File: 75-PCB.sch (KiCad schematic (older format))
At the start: 324 parts, among them J1 AVR-ISP-6, Q1 2N7002, SW1 SW_Push, U1 AT90USB1286-AU, U2 PRTR5V0U2X, Y1 16MHz

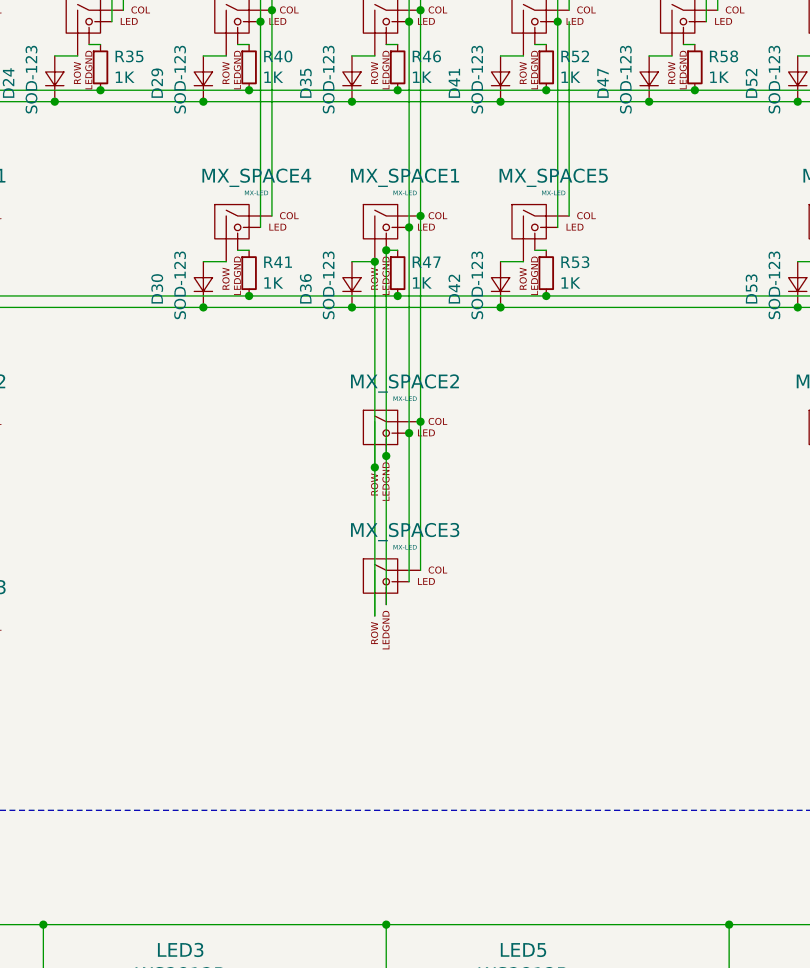
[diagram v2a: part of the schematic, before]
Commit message: Added switch for support for another bottom row layout
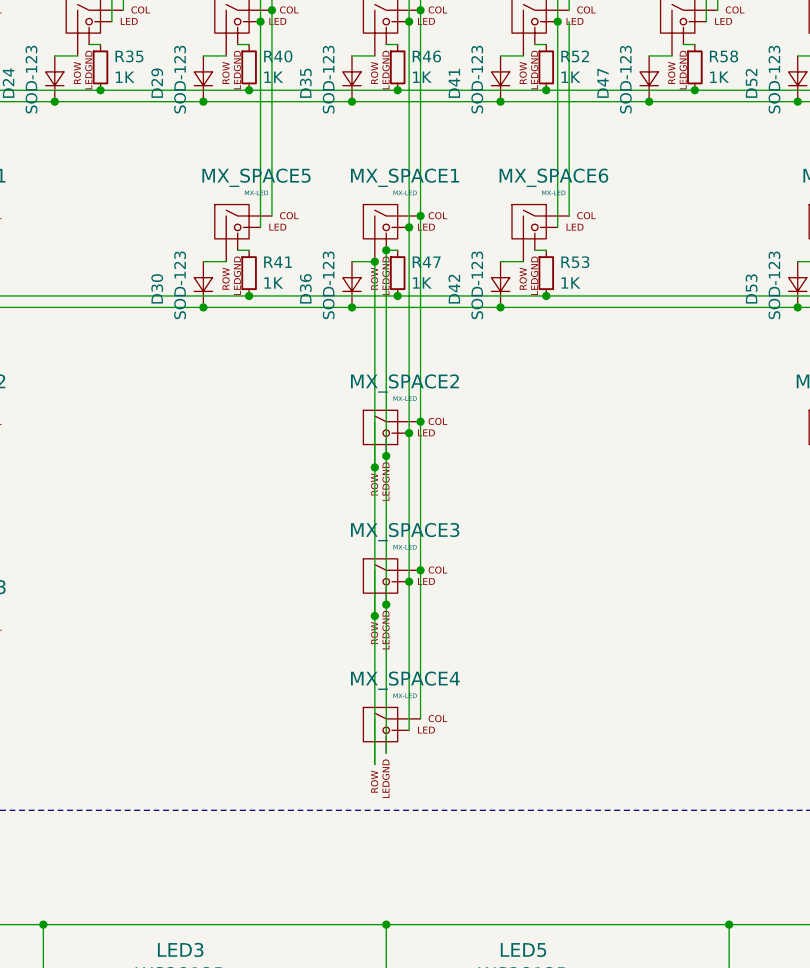
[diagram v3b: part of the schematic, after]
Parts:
- added MX_SPACE4: MX-LED, MX_Only:MXOnly-1.25U, symbol MX_Alps_Hybrid:MX-LED
- MX_SPACE3: footprint MX_Only:MXOnly-1.25U -> MX_Only:MXOnly-7U-FLIPPED-ReversedStabilizers
- renumbered MX_SPACE4 to MX_SPACE5, MX_SPACE5 to MX_SPACE6
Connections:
- net +5V: now also MX_SPACE4.3 (LED)
- net COL5: now also MX_SPACE4.1 (COL)
- net at D36.2 (A), MX_SPACE1.2 (ROW), MX_SPACE2.2 (ROW)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: now also MX_SPACE4.2 (ROW)
- net at MX_SPACE1.4 (LEDGND), MX_SPACE2.4 (LEDGND), MX_SPACE3.4 (LEDGND)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: now also MX_SPACE4.4 (LEDGND)
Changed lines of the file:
@@
 $EndComp
 $Comp
-L MX_Alps_Hybrid:MX-LED MX_SPACE4
+L MX_Alps_Hybrid:MX-LED MX_SPACE5
 U 1 1 5EA48DDC
 P 3850 5950
-F 0 "MX_SPACE4" H 3932 6174 60  0000 C CNN
+F 0 "MX_SPACE5" H 3932 6174 60  0000 C CNN
 F 1 "MX-LED" H 3932 6100 20  0000 C CNN
 F 2 "MX_Only:MXOnly-2.75U-ReversedStabilizers" H 3225 5925 60  0001 C CNN
@@
 Connection ~ 4450 6100
 $Comp
-L MX_Alps_Hybrid:MX-LED MX_SPACE5
+L MX_Alps_Hybrid:MX-LED MX_SPACE6
 U 1 1 5EE96CC6
 P 5150 5950
-F 0 "MX_SPACE5" H 5232 6174 60  0000 C CNN
+F 0 "MX_SPACE6" H 5232 6174 60  0000 C CNN
 F 1 "MX-LED" H 5232 6100 20  0000 C CNN
 F 2 "MX_Only:MXOnly-2.25U-ReversedStabilizers" H 4525 5925 60  0001 C CNN
@@
 F 0 "MX_SPACE3" H 4582 7724 60  0000 C CNN
 F 1 "MX-LED" H 4582 7650 20  0000 C CNN
-F 2 "MX_Only:MXOnly-1.25U" H 3875 7475 60  0001 C CNN
+F 2 "MX_Only:MXOnly-7U-FLIPPED-ReversedStabilizers" H 3875 7475 60  0001 C CNN
 F 3 "" H 3875 7475 60  0001 C CNN
 	1    4500 7500
@@
 	700  5200 1100 5200
 Connection ~ 1100 5200
-$Comp
-L MX_Alps_Hybrid:MX-LED MX_LCTRL3
-U 1 1 5F0D2C14
-P 1250 7750
-F 0 "MX_LCTRL3" H 1332 7974 60  0000 C CNN
-F 1 "MX-LED" H 1332 7900 20  0000 C CNN
-F 2 "MX_Only:MXOnly-1.5U" H 625 7725 60  0001 C CNN
-F 3 "" H 625 7725 60  0001 C CNN
-	1    1250 7750
-	1    0    0    -1
-$EndComp
-$Comp
-L MX_Alps_Hybrid:MX-LED MX_LALT3
-U 1 1 5F0D2C1A
-P 2550 7750
-F 0 "MX_LALT3" H 2632 7974 60  0000 C CNN
-F 1 "MX-LED" H 2632 7900 20  0000 C CNN
-F 2 "MX_Only:MXOnly-1.5U" H 1925 7725 60  0001 C CNN
-F 3 "" H 1925 7725 60  0001 C CNN
-	1    2550 7750
-	1    0    0    -1
-$EndComp
-Wire Wire Line
-	2700 7700 2700 6800
-Wire Wire Line
-	1400 7700 1400 6800
 $Comp
 L MX_Alps_Hybrid:MX-LED MX_LWIN2
@@
 	1850 6100 1850 7000
 Connection ~ 1850 6100
-Wire Wire Line
-	2500 7900 2500 7000
-Connection ~ 2500 7000
-Wire Wire Line
-	1200 7900 1200 7000
-Connection ~ 1200 7000
 $Comp
 L Device:R_Small R18
@@
 Connection ~ 1250 6050
 Wire Wire Line
-	1250 7850 1250 6950
-Connection ~ 1250 6950
-Wire Wire Line
-	2550 7850 2550 6950
-Wire Wire Line
 	2550 6950 2550 6050
-Connection ~ 2550 6950
 Connection ~ 2550 6050
 Wire Wire Line
@@
 Wire Wire Line
 	11050 6250 10400 6250
-Wire Wire Line
-	1350 7750 1350 6850
 Connection ~ 1350 1450
 Wire Wire Line
@@
 Wire Wire Line
 	1350 5950 1350 5050
-Connection ~ 1350 6850
 Wire Wire Line
 	1350 6850 1350 5950
@@
 	2000 5950 2000 6850
 Wire Wire Line
-	2650 7750 2650 6850
-Wire Wire Line
 	2650 1000 2000 1000
 Connection ~ 2650 1450
@@
 Wire Wire Line
 	2650 5950 2650 5050
-Connection ~ 2650 6850
 Wire Wire Line
 	2650 6850 2650 5950
@@
 Wire Wire Line
 	11100 5050 11100 5950
-Connection ~ 1400 6800
 Connection ~ 1750 5400
 Wire Wire Line
 	1750 5400 2400 5400
 Connection ~ 2050 5900
-Connection ~ 2700 6800
 Text GLabel 13400 4650 2    50   Input ~ 0
 RESET
@@
 	700  4300 1100 4300
 Connection ~ 1100 4300
+Connection ~ 2650 6850
+Wire Wire Line
+	2650 7750 2650 6850
+Connection ~ 1350 6850
+Wire Wire Line
+	1350 7750 1350 6850
+Connection ~ 2550 6950
+Wire Wire Line
+	2550 7850 2550 6950
+Connection ~ 1250 6950
+Wire Wire Line
+	1250 7850 1250 6950
+Connection ~ 1200 7000
+Wire Wire Line
+	1200 7900 1200 7000
+Connection ~ 2500 7000
+Wire Wire Line
+	2500 7900 2500 7000
+Connection ~ 1400 6800
+Wire Wire Line
+	1400 7700 1400 6800
+Connection ~ 2700 6800
+Wire Wire Line
+	2700 7700 2700 6800
+$Comp
+L MX_Alps_Hybrid:MX-LED MX_LALT3
+U 1 1 5F0D2C1A
+P 2550 7750
+F 0 "MX_LALT3" H 2632 7974 60  0000 C CNN
+F 1 "MX-LED" H 2632 7900 20  0000 C CNN
+F 2 "MX_Only:MXOnly-1.5U" H 1925 7725 60  0001 C CNN
+F 3 "" H 1925 7725 60  0001 C CNN
+	1    2550 7750
+	1    0    0    -1
+$EndComp
+$Comp
+L MX_Alps_Hybrid:MX-LED MX_LCTRL3
+U 1 1 5F0D2C14
+P 1250 7750
+F 0 "MX_LCTRL3" H 1332 7974 60  0000 C CNN
+F 1 "MX-LED" H 1332 7900 20  0000 C CNN
+F 2 "MX_Only:MXOnly-1.5U" H 625 7725 60  0001 C CNN
+F 3 "" H 625 7725 60  0001 C CNN
+	1    1250 7750
+	1    0    0    -1
+$EndComp
+$Comp
+L MX_Alps_Hybrid:MX-LED MX_SPACE4
+U 1 1 5EA67D89
+P 4500 8150
+F 0 "MX_SPACE4" H 4582 8374 60  0000 C CNN
+F 1 "MX-LED" H 4582 8300 20  0000 C CNN
+F 2 "MX_Only:MXOnly-1.25U" H 3875 8125 60  0001 C CNN
+F 3 "" H 3875 8125 60  0001 C CNN
+	1    4500 8150
+	1    0    0    -1
+$EndComp
+Wire Wire Line
+	4650 7450 4650 8100
+Wire Wire Line
+	4600 7500 4600 8150
+Wire Wire Line
+	4450 7650 4450 8300
+Wire Wire Line
+	4500 8250 4500 7600
+Connection ~ 4450 7650
+Connection ~ 4500 7600
+Connection ~ 4600 7500
+Connection ~ 4650 7450
 $EndSCHEMATC

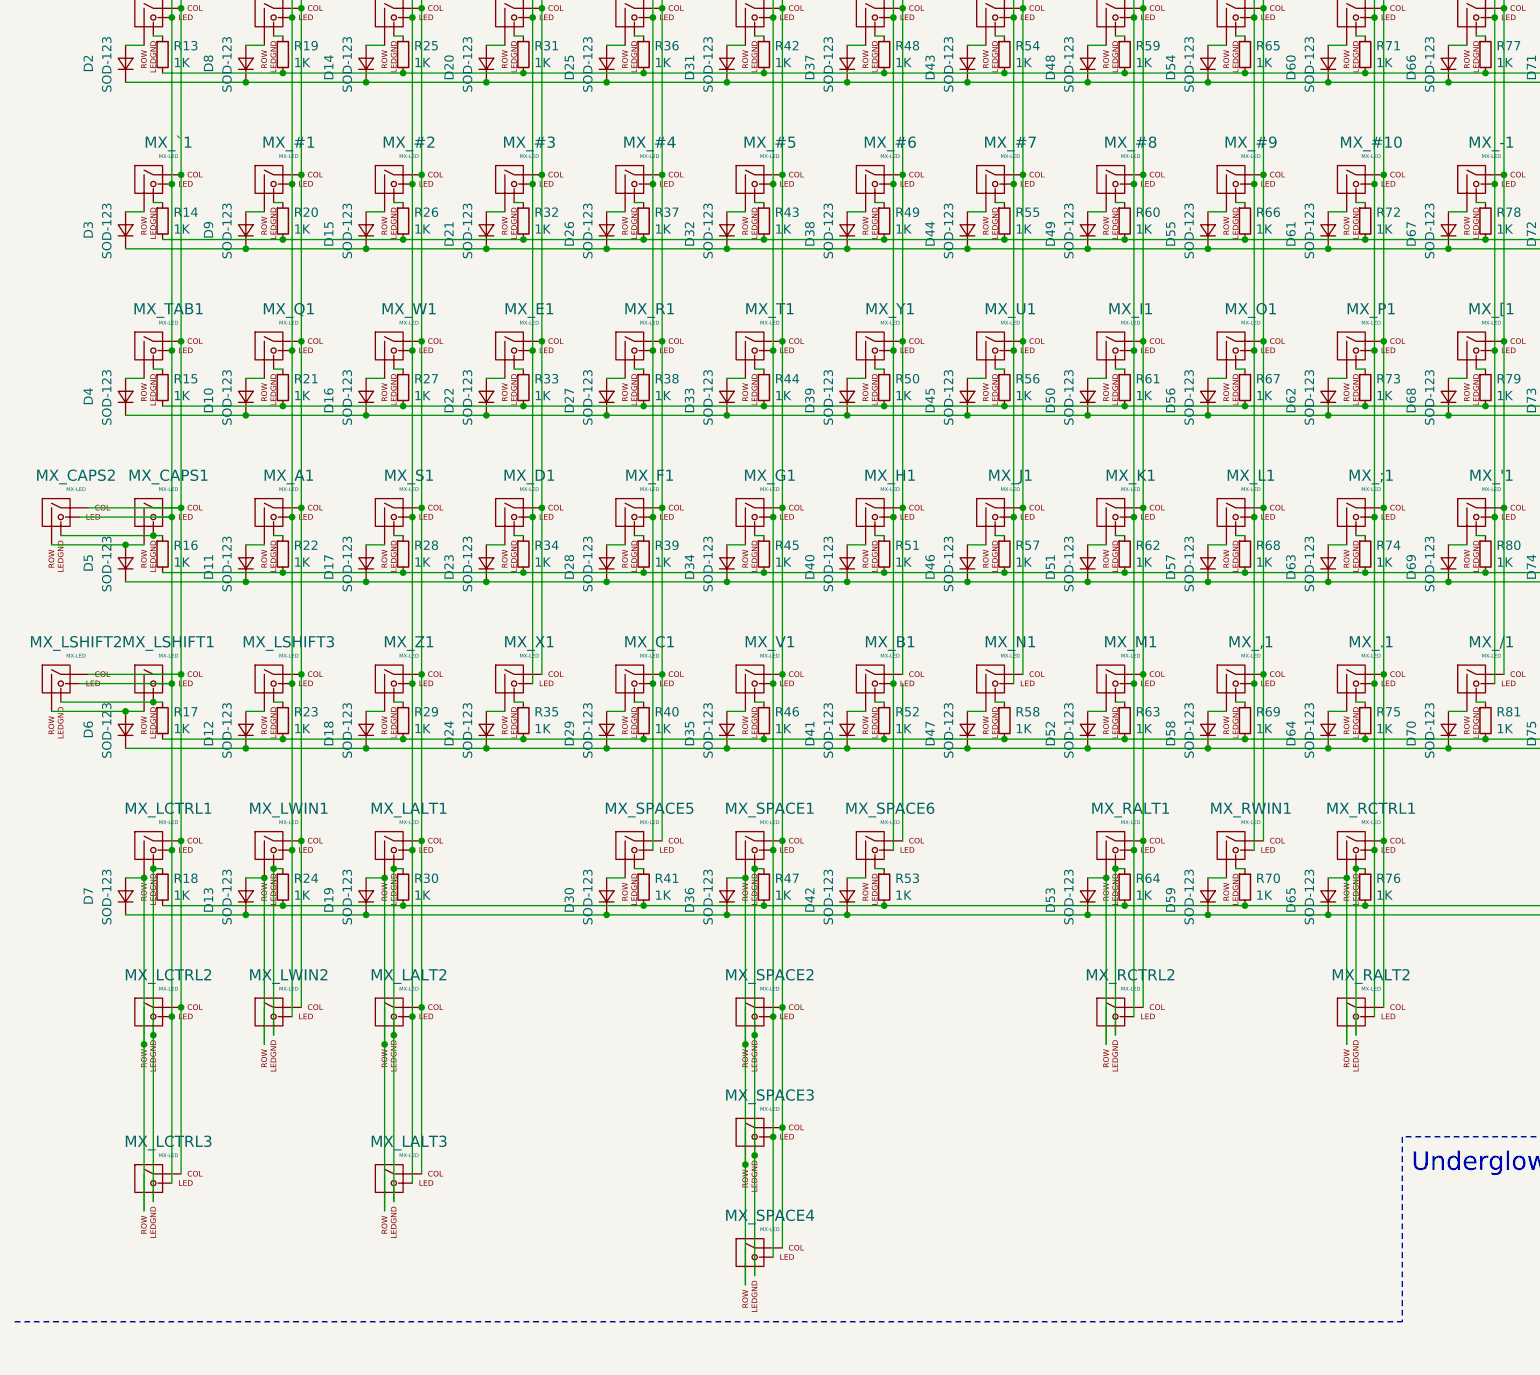
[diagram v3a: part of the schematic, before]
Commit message: Finished key layout in PCB file
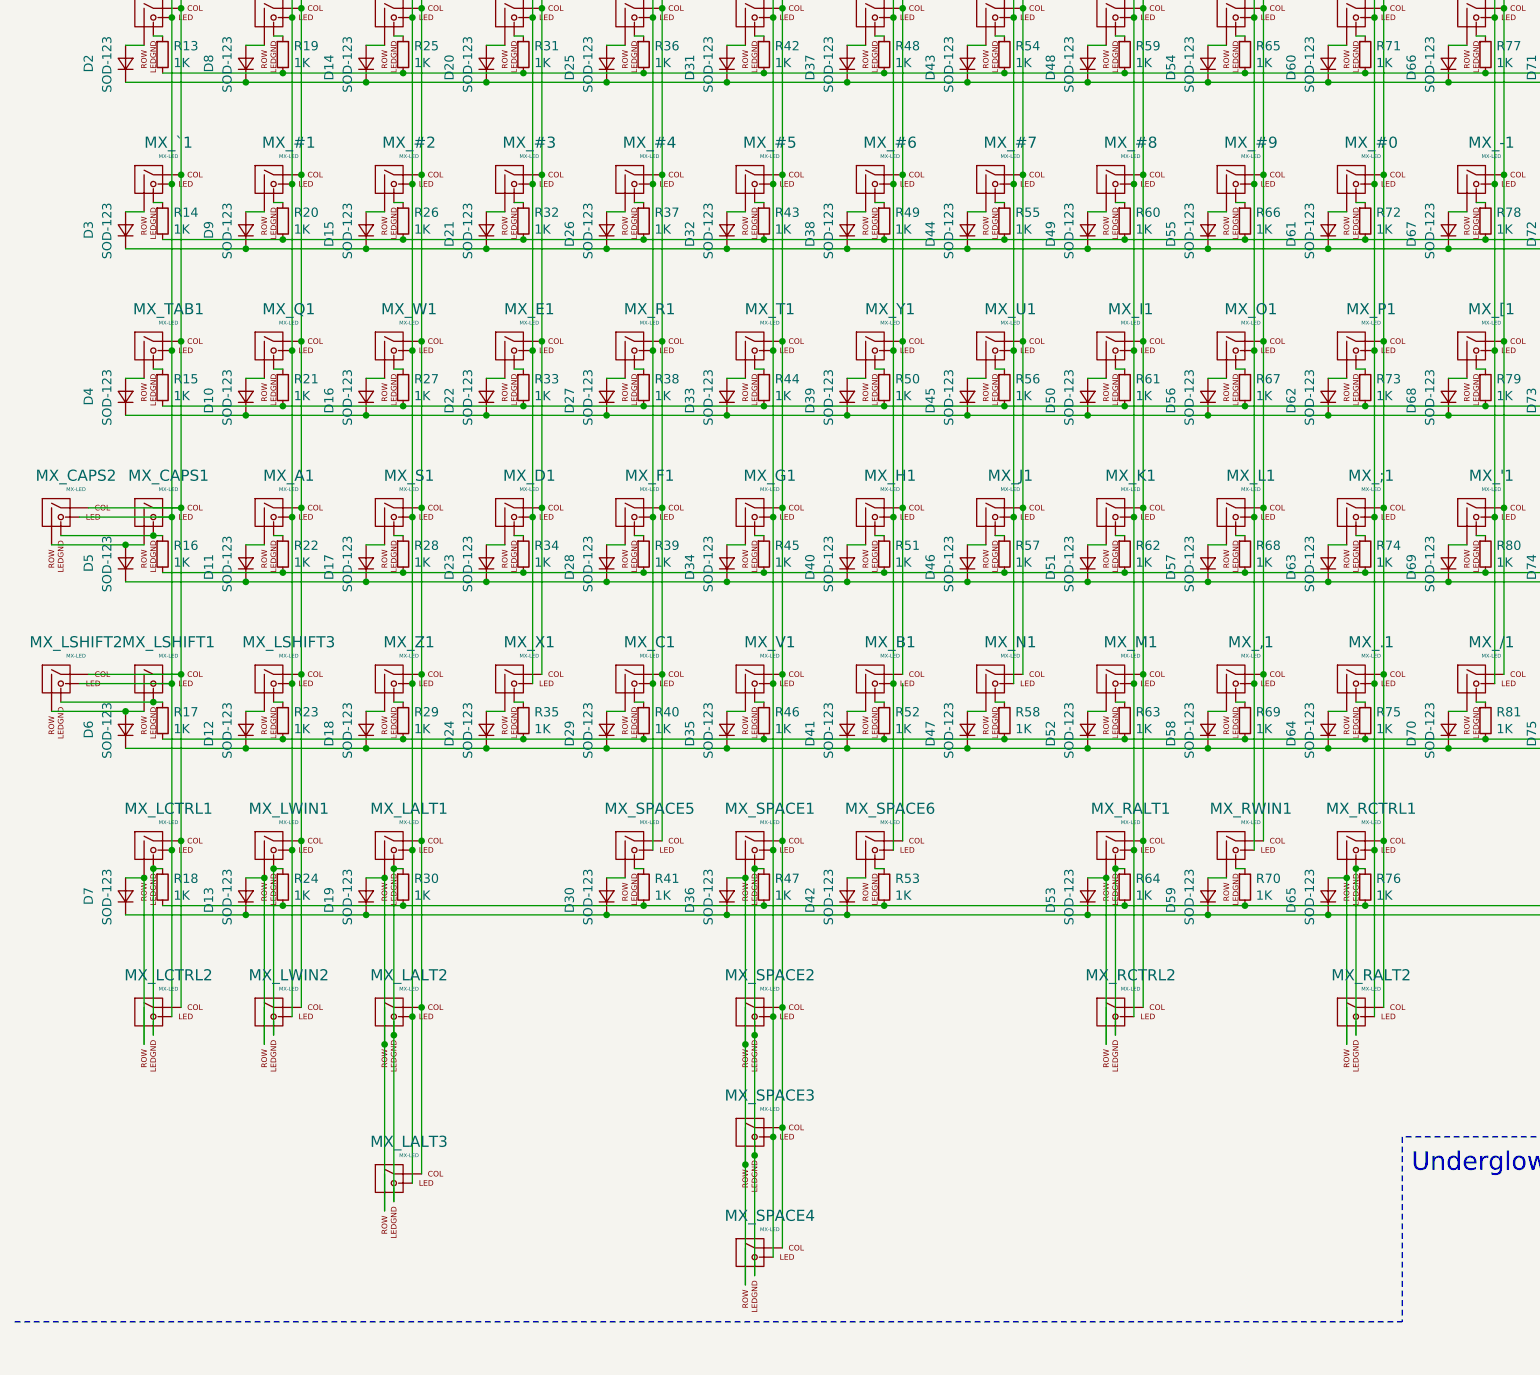
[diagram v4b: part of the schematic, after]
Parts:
- removed MX_LCTRL3: MX-LED, MX_Only:MXOnly-1.5U, symbol MX_Alps_Hybrid:MX-LED
- renumbered MX_#10 to MX_#0
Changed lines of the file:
@@
 $EndComp
 $Comp
-L MX_Alps_Hybrid:MX-LED MX_#10
+L MX_Alps_Hybrid:MX-LED MX_#0
 U 1 1 650B459E
 P 7750 2350
-F 0 "MX_#10" H 7832 2574 60  0000 C CNN
+F 0 "MX_#0" H 7832 2574 60  0000 C CNN
 F 1 "MX-LED" H 7832 2500 20  0000 C CNN
 F 2 "MX_Only:MXOnly-1U" H 7125 2325 60  0001 C CNN
@@
 Wire Wire Line
 	2650 7750 2650 6850
-Connection ~ 1350 6850
-Wire Wire Line
-	1350 7750 1350 6850
 Connection ~ 2550 6950
 Wire Wire Line
 	2550 7850 2550 6950
-Connection ~ 1250 6950
-Wire Wire Line
-	1250 7850 1250 6950
-Connection ~ 1200 7000
-Wire Wire Line
-	1200 7900 1200 7000
 Connection ~ 2500 7000
 Wire Wire Line
 	2500 7900 2500 7000
-Connection ~ 1400 6800
-Wire Wire Line
-	1400 7700 1400 6800
 Connection ~ 2700 6800
 Wire Wire Line
@@
 	1    0    0    -1
 $EndComp
-$Comp
-L MX_Alps_Hybrid:MX-LED MX_LCTRL3
-U 1 1 5F0D2C14
-P 1250 7750
-F 0 "MX_LCTRL3" H 1332 7974 60  0000 C CNN
-F 1 "MX-LED" H 1332 7900 20  0000 C CNN
-F 2 "MX_Only:MXOnly-1.5U" H 625 7725 60  0001 C CNN
-F 3 "" H 625 7725 60  0001 C CNN
-	1    1250 7750
-	1    0    0    -1
-$EndComp
